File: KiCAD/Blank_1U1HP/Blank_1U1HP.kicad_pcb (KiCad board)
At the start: 2 copper layers, 5 x 39.7 mm, 2 parts

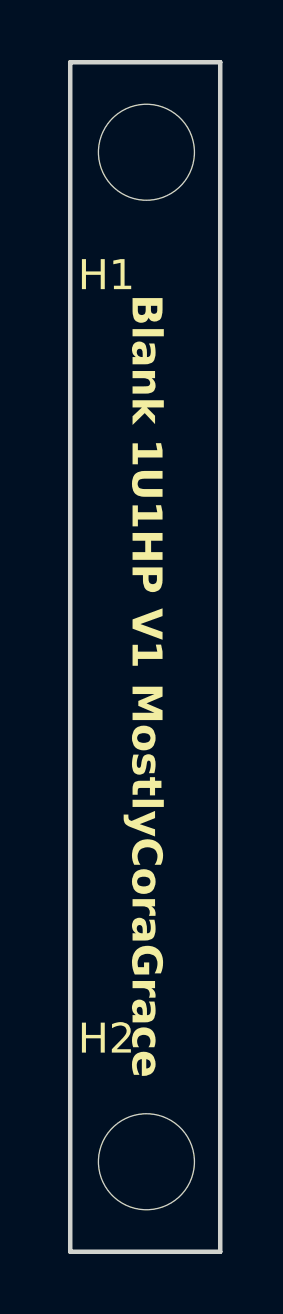
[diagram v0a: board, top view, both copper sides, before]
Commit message: removed all front silkscreen, and flipped most modules, to make the boards 'cleaner'.
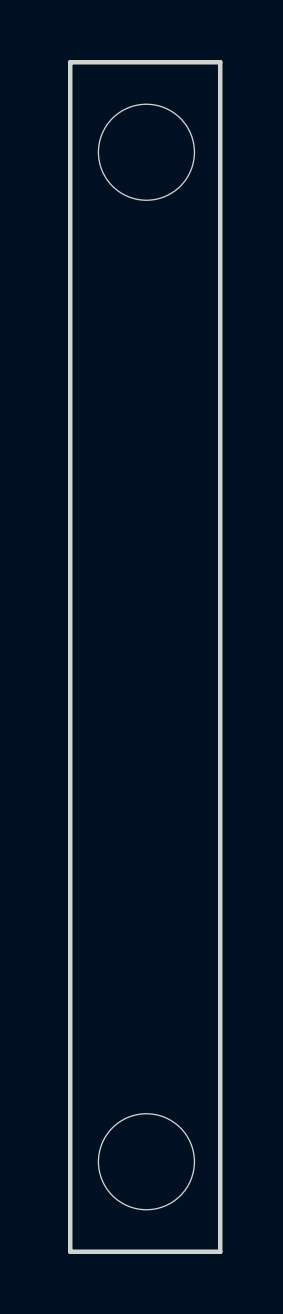
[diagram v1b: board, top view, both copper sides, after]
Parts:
- H1, H2: moved to B.Cu
- turned H1 to 180 degrees
- turned H2 to 180 degrees

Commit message: added copper fills to every module, to maybe possibly increase structural rigidity.
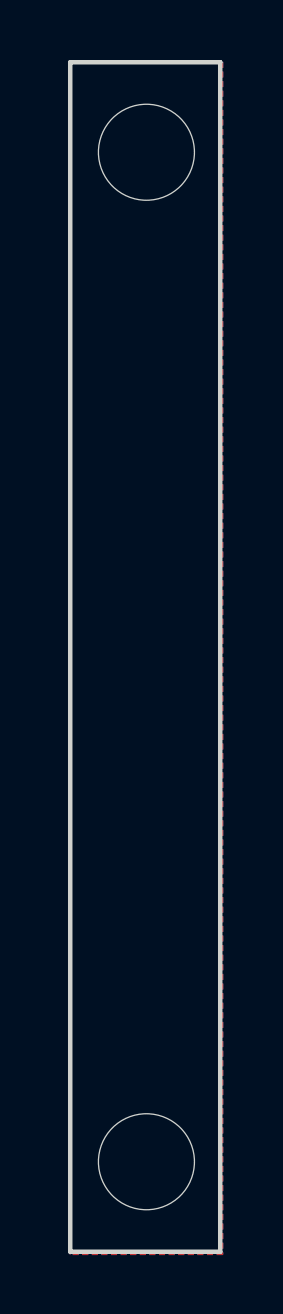
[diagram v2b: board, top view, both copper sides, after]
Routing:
- added copper zone on B.Cu, net (none)
- added copper zone on F.Cu, net (none)
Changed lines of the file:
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@@
+		)
+	)
+	(zone
+		(net 0)
+		(net_name "")
+		(layers "F&B.Cu")
+		(hatch edge 0.5)
+		(connect_pads
+			(clearance 0.5)
+		)
+		(min_thickness 0.25)
+		(filled_areas_thickness no)
+		(fill yes
+			(thermal_gap 0.5)
+			(thermal_bridge_width 0.5)
+			(island_removal_mode 1)
+			(island_area_min 10)
+		)
+		(polygon
+			(pts
+				(xy 0 2.413) (xy 5.08 2.413) (xy 5.08 42.164) (xy 0 42.164)
+			)
 		)
 	)

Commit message: added PCBWay print identification silkscreen text to each component
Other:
- board text added: "WayWayWay"
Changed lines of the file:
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@@
 		(layer "Edge.Cuts")
+	)
+	(gr_text "WayWayWay"
+		(at 3.25 10.75 90)
+		(layer "B.SilkS")
+		(effects
+			(font
+				(size 1 1)
+				(thickness 0.15)
+			)
+			(justify left top mirror)
+		)
 	)
 	(gr_text "Blank 1U1HP V1 MostlyCoraGrace"
